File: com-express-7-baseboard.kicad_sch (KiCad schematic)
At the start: 0 parts

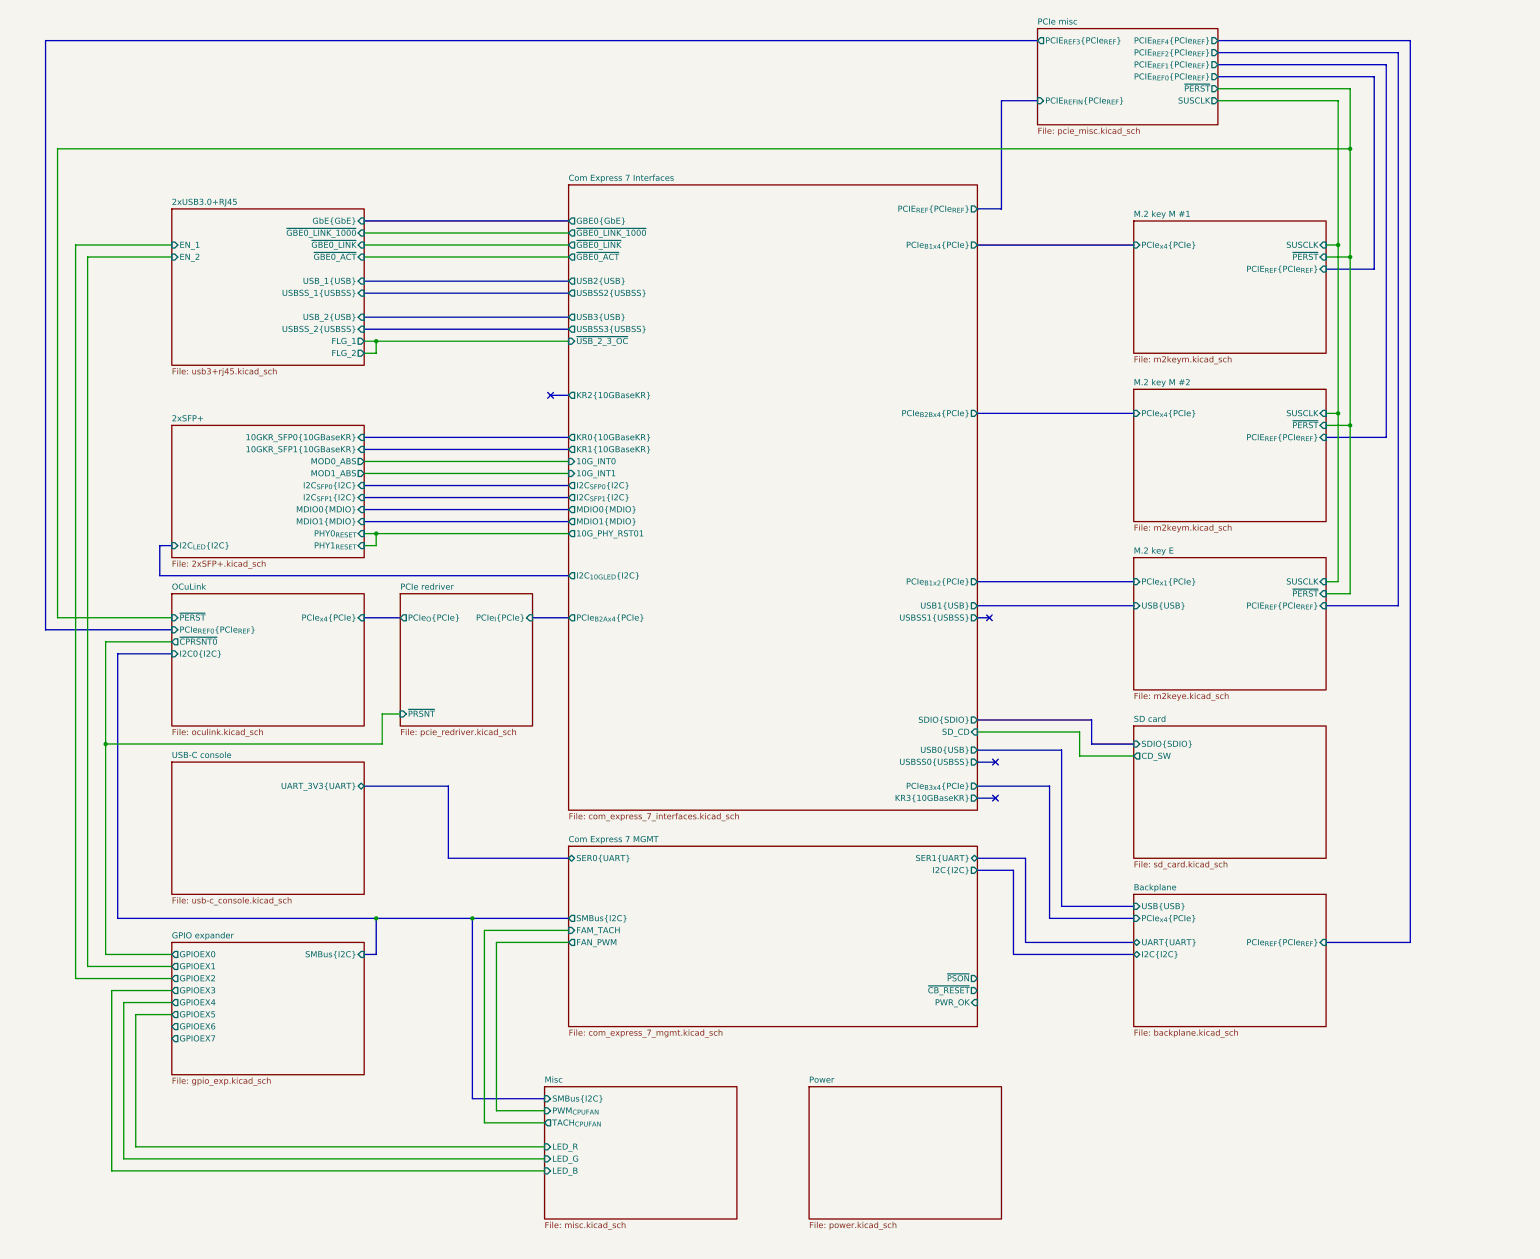
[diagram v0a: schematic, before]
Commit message: [#58137] Add power sequencing and reset
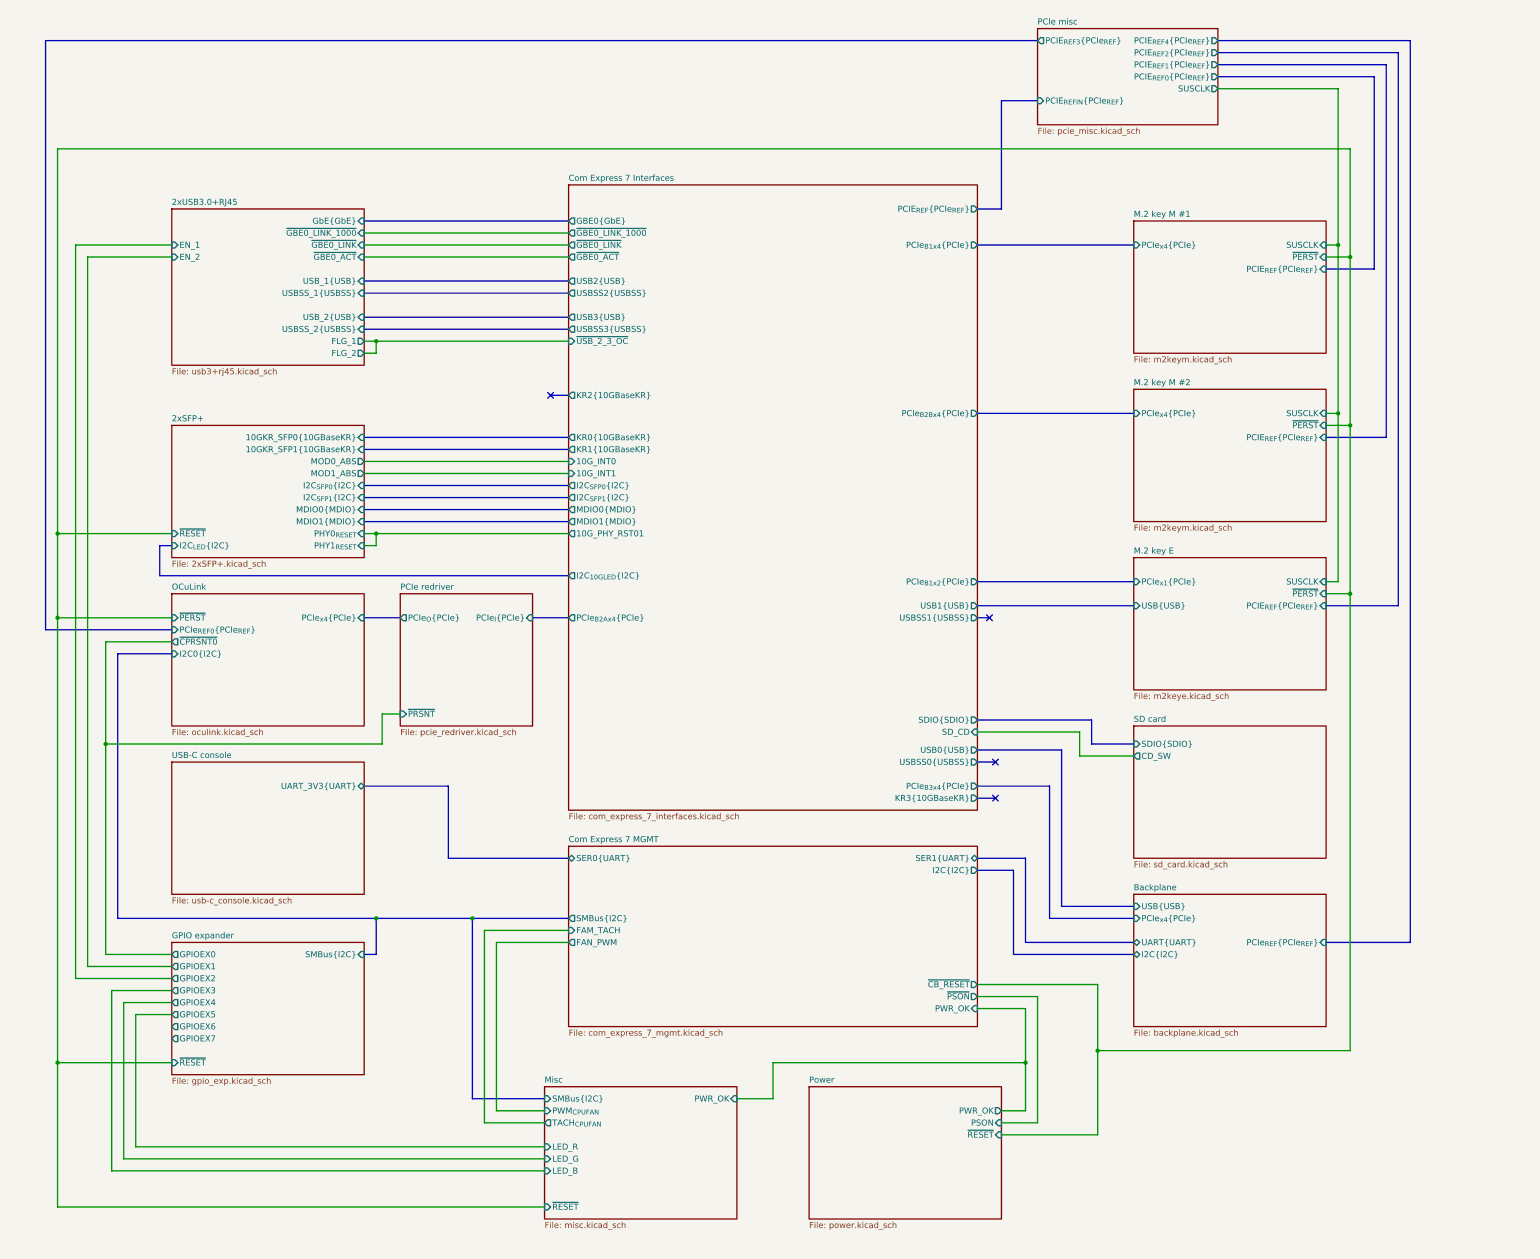
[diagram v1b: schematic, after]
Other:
- sheet 2xSFP+ ports: added ~{RESET}; removed none
- sheet GPIO expander ports: added ~{RESET}; removed none
- sheet Misc ports: added PWR_OK, ~{RESET}; removed none
- sheet PCIe misc ports: added none; removed ~{PERST}
- sheet Power ports: added PSON, PWR_OK, ~{RESET}; removed none
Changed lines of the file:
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@@
   (bus_alias "USB" (members "D+" "D-"))
   (bus_alias "USBSS" (members "TX+" "TX-" "RX+" "RX-"))
-  (junction (at 327.66 45.72) (diameter 0) (color 0 0 0 0)
-  )
   (junction (at 325.12 66.04) (diameter 0) (color 0 0 0 0)
   )
+  (junction (at 54.61 238.76) (diameter 0) (color 0 0 0 0)
+  )
+  (junction (at 327.66 139.7) (diameter 0) (color 0 0 0 0)
+  )
   (junction (at 121.92 86.36) (diameter 0) (color 0 0 0 0)
   )
+  (junction (at 274.32 236.22) (diameter 0) (color 0 0 0 0)
+  )
   (junction (at 121.92 208.28) (diameter 0) (color 0 0 0 0)
   )
   (junction (at 327.66 104.14) (diameter 0) (color 0 0 0 0)
   )
+  (junction (at 54.61 127) (diameter 0) (color 0 0 0 0)
+  )
   (junction (at 325.12 101.6) (diameter 0) (color 0 0 0 0)
   )
   (junction (at 142.24 208.28) (diameter 0) (color 0 0 0 0)
   )
+  (junction (at 54.61 144.78) (diameter 0) (color 0 0 0 0)
+  )
   (junction (at 64.77 171.45) (diameter 0) (color 0 0 0 0)
   )
   (junction (at 121.92 127) (diameter 0) (color 0 0 0 0)
+  )
+  (junction (at 259.08 238.76) (diameter 0) (color 0 0 0 0)
   )
   (junction (at 327.66 68.58) (diameter 0) (color 0 0 0 0)
@@
     (stroke (width 0) (type default) (color 255 153 0 1))
   )
+  (wire (pts (xy 248.92 222.25) (xy 274.32 222.25))
+    (stroke (width 0) (type default))
+  )
   (bus (pts (xy 299.72 27.94) (xy 335.28 27.94))
     (stroke (width 0) (type default))
@@
     (stroke (width 0) (type default) (color 0 255 255 1))
   )
+  (wire (pts (xy 248.92 227.33) (xy 259.08 227.33))
+    (stroke (width 0) (type default))
+  )
   (bus (pts (xy 119.38 60.96) (xy 162.56 60.96))
     (stroke (width 0) (type default))
@@
     (stroke (width 0) (type default))
   )
-  (wire (pts (xy 54.61 45.72) (xy 54.61 144.78))
+  (wire (pts (xy 54.61 45.72) (xy 54.61 127))
     (stroke (width 0) (type default))
   )
@@
     (stroke (width 0) (type default) (color 255 153 0 1))
   )
-  (wire (pts (xy 299.72 33.02) (xy 327.66 33.02))
-    (stroke (width 0) (type default))
-  )
   (bus (pts (xy 266.7 205.74) (xy 281.94 205.74))
     (stroke (width 0) (type default) (color 0 0 255 1))
@@
     (stroke (width 0) (type default))
   )
+  (wire (pts (xy 205.74 238.76) (xy 259.08 238.76))
+    (stroke (width 0) (type default))
+  )
+  (wire (pts (xy 54.61 144.78) (xy 54.61 238.76))
+    (stroke (width 0) (type default))
+  )
   (wire (pts (xy 119.38 86.36) (xy 121.92 86.36))
     (stroke (width 0) (type default))
   )
   (wire (pts (xy 71.12 228.6) (xy 78.74 228.6))
+    (stroke (width 0) (type default))
+  )
+  (wire (pts (xy 198.12 246.38) (xy 205.74 246.38))
     (stroke (width 0) (type default))
   )
@@
     (stroke (width 0) (type default))
   )
+  (wire (pts (xy 54.61 127) (xy 54.61 144.78))
+    (stroke (width 0) (type default))
+  )
   (wire (pts (xy 325.12 137.16) (xy 322.58 137.16))
+    (stroke (width 0) (type default))
+  )
+  (wire (pts (xy 261.62 251.46) (xy 261.62 224.79))
     (stroke (width 0) (type default))
   )
@@
     (stroke (width 0) (type default) (color 0 0 255 1))
   )
+  (wire (pts (xy 274.32 222.25) (xy 274.32 236.22))
+    (stroke (width 0) (type default))
+  )
   (wire (pts (xy 78.74 149.86) (xy 64.77 149.86))
     (stroke (width 0) (type default))
@@
     (stroke (width 0) (type default) (color 194 0 194 1))
   )
-  (wire (pts (xy 299.72 35.56) (xy 325.12 35.56))
+  (wire (pts (xy 299.72 33.02) (xy 325.12 33.02))
     (stroke (width 0) (type default))
   )
@@
     (stroke (width 0) (type default))
   )
+  (wire (pts (xy 54.61 127) (xy 78.74 127))
+    (stroke (width 0) (type default))
+  )
   (wire (pts (xy 119.38 127) (xy 121.92 127))
     (stroke (width 0) (type default))
@@
     (stroke (width 0) (type default))
   )
+  (wire (pts (xy 327.66 236.22) (xy 327.66 139.7))
+    (stroke (width 0) (type default))
+  )
   (bus (pts (xy 299.72 25.4) (xy 337.82 25.4))
     (stroke (width 0) (type default))
@@
   )
   (wire (pts (xy 58.42 66.04) (xy 58.42 220.98))
+    (stroke (width 0) (type default))
+  )
+  (wire (pts (xy 274.32 236.22) (xy 327.66 236.22))
     (stroke (width 0) (type default))
   )
@@
     (stroke (width 0) (type default))
   )
+  (wire (pts (xy 274.32 254) (xy 274.32 236.22))
+    (stroke (width 0) (type default))
+  )
   (wire (pts (xy 327.66 68.58) (xy 327.66 45.72))
     (stroke (width 0) (type default))
@@
   )
   (wire (pts (xy 327.66 139.7) (xy 327.66 104.14))
+    (stroke (width 0) (type default))
+  )
+  (wire (pts (xy 261.62 224.79) (xy 248.92 224.79))
     (stroke (width 0) (type default))
   )
@@
     (stroke (width 0) (type default))
   )
+  (wire (pts (xy 259.08 227.33) (xy 259.08 238.76))
+    (stroke (width 0) (type default))
+  )
   (wire (pts (xy 119.38 63.5) (xy 162.56 63.5))
     (stroke (width 0) (type default))
@@
     (stroke (width 0) (type default))
   )
-  (wire (pts (xy 325.12 66.04) (xy 325.12 35.56))
+  (wire (pts (xy 259.08 238.76) (xy 259.08 248.92))
+    (stroke (width 0) (type default))
+  )
+  (wire (pts (xy 325.12 66.04) (xy 325.12 33.02))
     (stroke (width 0) (type default))
   )
@@
     (stroke (width 0) (type default))
   )
-  (wire (pts (xy 327.66 33.02) (xy 327.66 45.72))
-    (stroke (width 0) (type default))
-  )
   (bus (pts (xy 142.24 246.38) (xy 142.24 208.28))
     (stroke (width 0) (type default))
@@
     (stroke (width 0) (type default))
   )
+  (wire (pts (xy 78.74 238.76) (xy 54.61 238.76))
+    (stroke (width 0) (type default))
+  )
   (bus (pts (xy 256.54 215.9) (xy 281.94 215.9))
     (stroke (width 0) (type default))
   )
+  (wire (pts (xy 254 254) (xy 274.32 254))
+    (stroke (width 0) (type default))
+  )
+  (wire (pts (xy 259.08 248.92) (xy 254 248.92))
+    (stroke (width 0) (type default))
+  )
+  (wire (pts (xy 254 251.46) (xy 261.62 251.46))
+    (stroke (width 0) (type default))
+  )
   (wire (pts (xy 119.38 88.9) (xy 121.92 88.9))
+    (stroke (width 0) (type default))
+  )
+  (wire (pts (xy 54.61 269.24) (xy 54.61 238.76))
+    (stroke (width 0) (type default))
+  )
+  (wire (pts (xy 205.74 246.38) (xy 205.74 238.76))
     (stroke (width 0) (type default))
   )
@@
     (stroke (width 0) (type default) (color 255 0 0 1))
   )
+  (wire (pts (xy 157.48 269.24) (xy 54.61 269.24))
+    (stroke (width 0) (type default))
+  )
   (bus (pts (xy 256.54 198.12) (xy 256.54 215.9))
     (stroke (width 0) (type default))
@@
       (effects (font (size 1.27 1.27)) (justify left))
     )
-    (pin "~{PERST}" output (at 299.72 33.02 0)
-      (effects (font (size 1.27 1.27)) (justify right))
-    )
-    (pin "SUSCLK" output (at 299.72 35.56 0)
+    (pin "SUSCLK" output (at 299.72 33.02 0)
       (effects (font (size 1.27 1.27)) (justify right))
     )
@@
       (effects (font (size 1.27 1.27)) (justify left))
     )
+    (pin "~{RESET}" input (at 78.74 238.76 180)
+      (effects (font (size 1.27 1.27)) (justify left))
+    )
     (instances
       (project "com-express-7-baseboard"
@@
       (effects (font (size 1.27 1.27)) (justify left))
     )
+    (pin "~{RESET}" input (at 157.48 269.24 180)
+      (effects (font (size 1.27 1.27)) (justify left))
+    )
+    (pin "PWR_OK" input (at 198.12 246.38 0)
+      (effects (font (size 1.27 1.27)) (justify right))
+    )
     (instances
       (project "com-express-7-baseboard"
@@
       (effects (font (size 1.27 1.27)) (justify left top))
     )
+    (pin "PWR_OK" output (at 254 248.92 0)
+      (effects (font (size 1.27 1.27)) (justify right))
+    )
+    (pin "PSON" input (at 254 251.46 0)
+      (effects (font (size 1.27 1.27)) (justify right))
+    )
+    (pin "~{RESET}" input (at 254 254 0)
+      (effects (font (size 1.27 1.27)) (justify right))
+    )
     (instances
       (project "com-express-7-baseboard"
@@
       (effects (font (size 1.27 1.27)) (justify left))
     )
+    (pin "~{RESET}" input (at 78.74 127 180)
+      (effects (font (size 1.27 1.27)) (justify left))
+    )
     (instances
       (project "com-express-7-baseboard"
@@
       (effects (font (size 1.27 1.27)) (justify left))
     )
-    (pin "~{PSON}" output (at 248.92 220.98 0)
+    (pin "~{PSON}" output (at 248.92 224.79 0)
       (effects (font (size 1.27 1.27)) (justify right))
     )
@@
       (effects (font (size 1.27 1.27)) (justify left))
     )
-    (pin "~{CB_RESET}" output (at 248.92 223.52 0)
-      (effects (font (size 1.27 1.27)) (justify right))
-    )
-    (pin "PWR_OK" input (at 248.92 226.06 0)
-      (effects (font (size 1.27 1.27)) (justify right))
-    )
+    (pin "~{CB_RESET}" output (at 248.92 222.25 0)
+      (effects (font (size 1.27 1.27)) (justify right))
+    )
+    (pin "PWR_OK" input (at 248.92 227.33 0)
+      (effects (font (size 1.27 1.27)) (justify right))
+    )

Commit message: Fix ERC
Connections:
- no-connect marks 4 -> 2
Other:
- sheet Backplane ports: added none; removed I2C{I2C}
- sheet Com Express 7 Interfaces ports: added none; removed KR2{10GBaseKR}, KR3{10GBaseKR}, USBSS0{USBSS}, USBSS1{USBSS}
- sheet Com Express 7 MGMT ports: added PSON; removed I2C{I2C}, ~{PSON}
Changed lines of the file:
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@@
   (junction (at 327.66 68.58) (diameter 0) (color 0 0 0 0)
   )
-  (no_connect (at 251.46 144.78))
-  (no_connect (at 158.75 97.79))
-  (no_connect (at 252.73 175.26))
-  (no_connect (at 252.73 182.88))
+  (no_connect (at 76.2 231.14))
+  (no_connect (at 76.2 233.68))
   (bus (pts (xy 259.08 213.36) (xy 281.94 213.36))
     (stroke (width 0) (type default) (color 255 153 0 1))
@@
     (stroke (width 0) (type default))
   )
-  (bus (pts (xy 248.92 144.78) (xy 251.46 144.78))
-    (stroke (width 0) (type default))
-  )
   (bus (pts (xy 248.92 195.58) (xy 259.08 195.58))
     (stroke (width 0) (type default) (color 255 153 0 1))
@@
     (stroke (width 0) (type default))
   )
-  (bus (pts (xy 248.92 175.26) (xy 252.73 175.26))
-    (stroke (width 0) (type default) (color 0 255 255 1))
-  )
   (wire (pts (xy 78.74 218.44) (xy 60.96 218.44))
     (stroke (width 0) (type default))
@@
   (bus (pts (xy 299.72 30.48) (xy 332.74 30.48))
     (stroke (width 0) (type default))
-  )
-  (bus (pts (xy 158.75 97.79) (xy 162.56 97.79))
-    (stroke (width 0) (type default) (color 255 0 0 1))
   )
   (wire (pts (xy 123.19 165.1) (xy 127 165.1))
@@
     (stroke (width 0) (type default))
   )
+  (wire (pts (xy 76.2 231.14) (xy 78.74 231.14))
+    (stroke (width 0) (type default))
+  )
   (wire (pts (xy 119.38 127) (xy 121.92 127))
     (stroke (width 0) (type default))
@@
     (stroke (width 0) (type default))
   )
-  (bus (pts (xy 248.92 198.12) (xy 256.54 198.12))
-    (stroke (width 0) (type default))
-  )
   (wire (pts (xy 157.48 259.08) (xy 68.58 259.08))
     (stroke (width 0) (type default))
@@
     (stroke (width 0) (type default))
   )
-  (bus (pts (xy 248.92 182.88) (xy 252.73 182.88))
-    (stroke (width 0) (type default))
-  )
   (wire (pts (xy 157.48 256.54) (xy 71.12 256.54))
     (stroke (width 0) (type default))
@@
     (stroke (width 0) (type default))
   )
-  (bus (pts (xy 256.54 215.9) (xy 281.94 215.9))
-    (stroke (width 0) (type default))
-  )
   (wire (pts (xy 254 254) (xy 274.32 254))
     (stroke (width 0) (type default))
@@
   )
   (wire (pts (xy 254 251.46) (xy 261.62 251.46))
+    (stroke (width 0) (type default))
+  )
+  (wire (pts (xy 76.2 233.68) (xy 78.74 233.68))
     (stroke (width 0) (type default))
   )
@@
     (stroke (width 0) (type default))
   )
-  (bus (pts (xy 256.54 198.12) (xy 256.54 215.9))
-    (stroke (width 0) (type default))
-  )
   (bus (pts (xy 266.7 172.72) (xy 266.7 205.74))
     (stroke (width 0) (type default) (color 0 0 255 1))
@@
       (effects (font (size 1.27 1.27)) (justify right))
     )
-    (pin "I2C{I2C}" bidirectional (at 281.94 215.9 180)
-      (effects (font (size 1.27 1.27)) (justify left))
-    )
     (instances
       (project "com-express-7-baseboard"
@@
       (effects (font (size 1.27 1.27)) (justify left))
     )
-    (pin "KR3{10GBaseKR}" output (at 248.92 182.88 0)
-      (effects (font (size 1.27 1.27)) (justify right))
-    )
-    (pin "KR2{10GBaseKR}" output (at 162.56 97.79 180)
-      (effects (font (size 1.27 1.27)) (justify left))
-    )
     (pin "PCIe_{B3x4}{PCIe}" output (at 248.92 180.34 0)
       (effects (font (size 1.27 1.27)) (justify right))
@@
       (effects (font (size 1.27 1.27)) (justify left))
     )
-    (pin "USBSS1{USBSS}" output (at 248.92 144.78 0)
-      (effects (font (size 1.27 1.27)) (justify right))
-    )
-    (pin "USBSS0{USBSS}" output (at 248.92 175.26 0)
-      (effects (font (size 1.27 1.27)) (justify right))
-    )
     (pin "~{GBE0_ACT}" output (at 162.56 68.58 180)
       (effects (font (size 1.27 1.27)) (justify left))
@@
       (effects (font (size 1.27 1.27)) (justify left))
     )
-    (pin "~{PSON}" output (at 248.92 224.79 0)
-      (effects (font (size 1.27 1.27)) (justify right))
-    )
     (pin "FAN_PWM" output (at 162.56 213.36 180)
       (effects (font (size 1.27 1.27)) (justify left))
@@
       (effects (font (size 1.27 1.27)) (justify right))
     )
-    (pin "I2C{I2C}" output (at 248.92 198.12 0)
-      (effects (font (size 1.27 1.27)) (justify right))
-    )
     (pin "SER0{UART}" bidirectional (at 162.56 195.58 180)
       (effects (font (size 1.27 1.27)) (justify left))
@@
       (effects (font (size 1.27 1.27)) (justify right))
     )
+    (pin "PSON" output (at 248.92 224.79 0)
+      (effects (font (size 1.27 1.27)) (justify right))
+    )
